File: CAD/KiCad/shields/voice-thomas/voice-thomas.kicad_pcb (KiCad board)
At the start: 2 copper layers, 30 x 42 mm, 20 parts

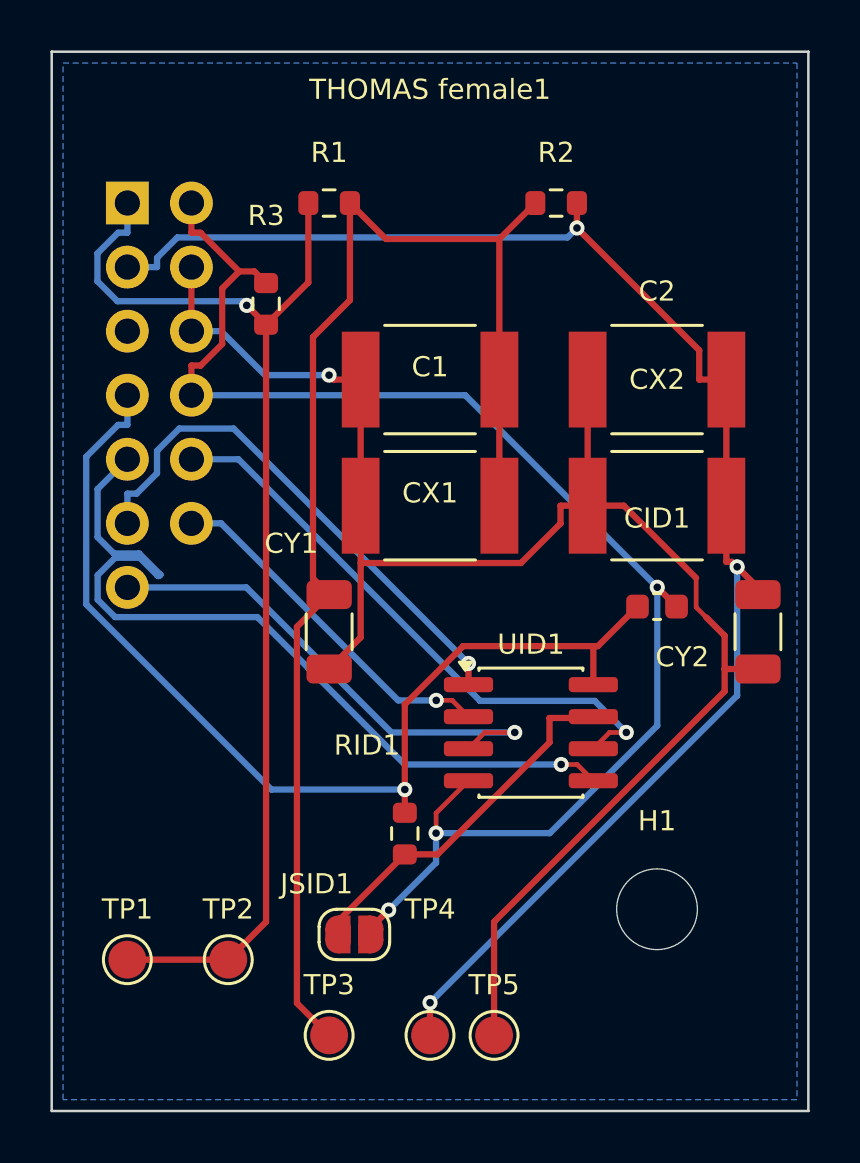
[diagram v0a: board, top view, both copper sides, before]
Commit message: Remove shield identification and adopt the simplified connector and Teensy pin maps
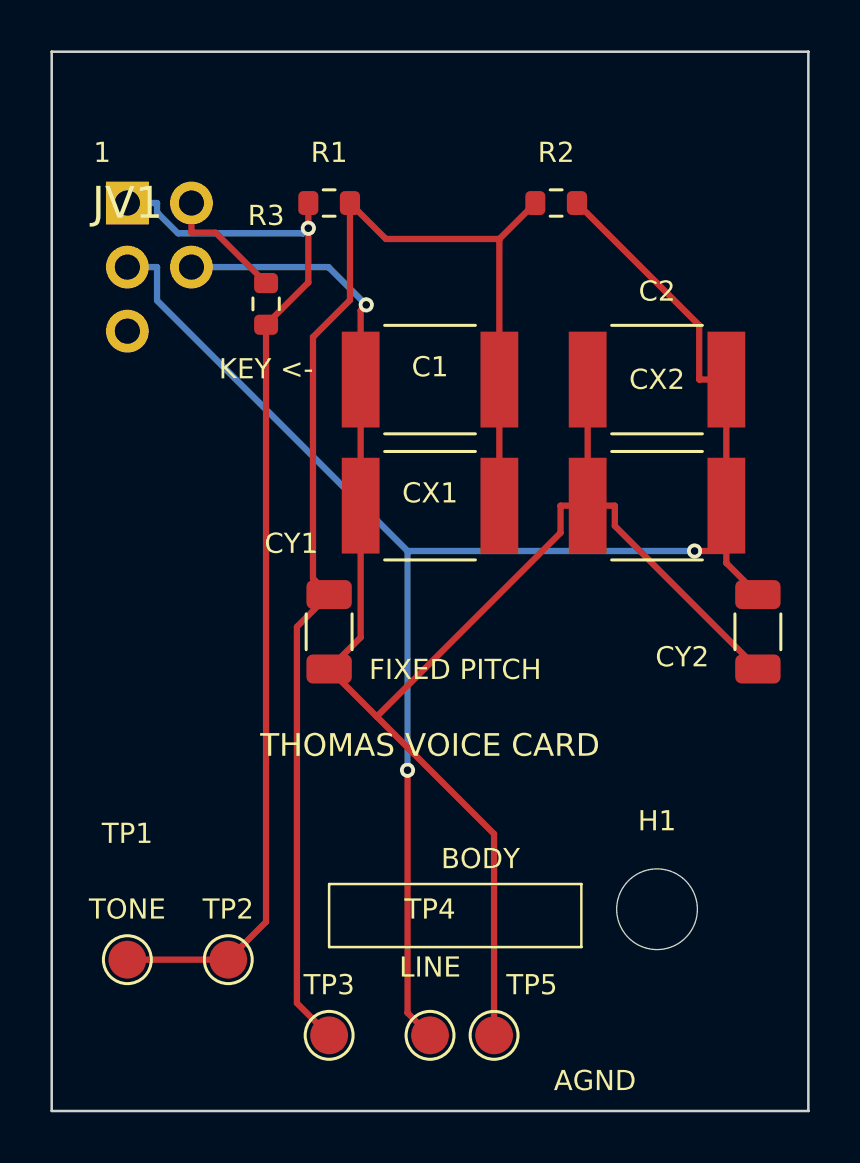
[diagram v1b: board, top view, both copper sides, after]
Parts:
- removed CID1: 100nF, Shields:C_0603_1608Metric
- removed JSID1: WRITE ENABLE - OPEN, Shields:SolderJumper-2_P1.3mm_Open_RoundedPad1.0x1.5mm
- removed RID1: 10K, Shields:R_0603_1608Metric
- removed UID1: M24C02-RMN6TP, Shields:SOIC-8_3.9x4.9mm_P1.27mm
- JV1: value VOICE - KEY 14 -> VOICE - KEY 6; footprint Shields:Socket_2x07_Key14 -> Shields:Socket_2x03_Key6
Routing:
- net GND: track 57.3 -> 4.96 mm, vias 3 -> 0
- net IOREF: track 41.5 -> 0.00 mm, vias 1 -> 0
- net shield/sda: track 33.4 -> 0.00 mm, vias 1 -> 0
- net shield/scl: track 23.3 -> 0.00 mm, vias 1 -> 0
- net addr0: track 21.0 -> 0.00 mm, vias 1 -> 0
- net addr2: track 19.8 -> 0.00 mm, vias 1 -> 0
- net id/wp: track 14.6 -> 0.00 mm
- net addr1: track 14.2 -> 0.00 mm, vias 1 -> 0
- net filter out: track 61.6 -> 67.9 mm, vias 3 -> 2
- net tone: track 46.5 -> 43.3 mm
- net AGND: track 66.6 -> 67.2 mm
- removed copper zone on B.Cu, net AGND
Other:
- board text added: "1"
- board text added: "1.2K"
- board text added: "1.8K"
- board text added: "10n"
- board text added: "150n"
- board text added: "2.2K"
- board text added: "220n"
- board text added: "2K"
- board text added: "470n"
- board text added: "47n"
- board text added: "AGND"
- board text added: "BODY"
- board text added: "BODY/Hz"
- board text added: "C1=C2"
- board text added: "F1 1012"
- board text added: "F2 2531"
- board text added: "F3 6329"
- board text added: "FIT"
- board text added: "FIXED PITCH"
- board text added: "KEY <-"
- board text added: "LINE"
- board text added: "M1 162"
- board text added: "M2 405"
- board text added: "R1=R2"
- board text added: "THOMAS VOICE CARD"
- board text added: "TONE"
- board text removed: "THOMAS female1"

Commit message: Finish revised shield routing, printed identification and clean KiCad checks
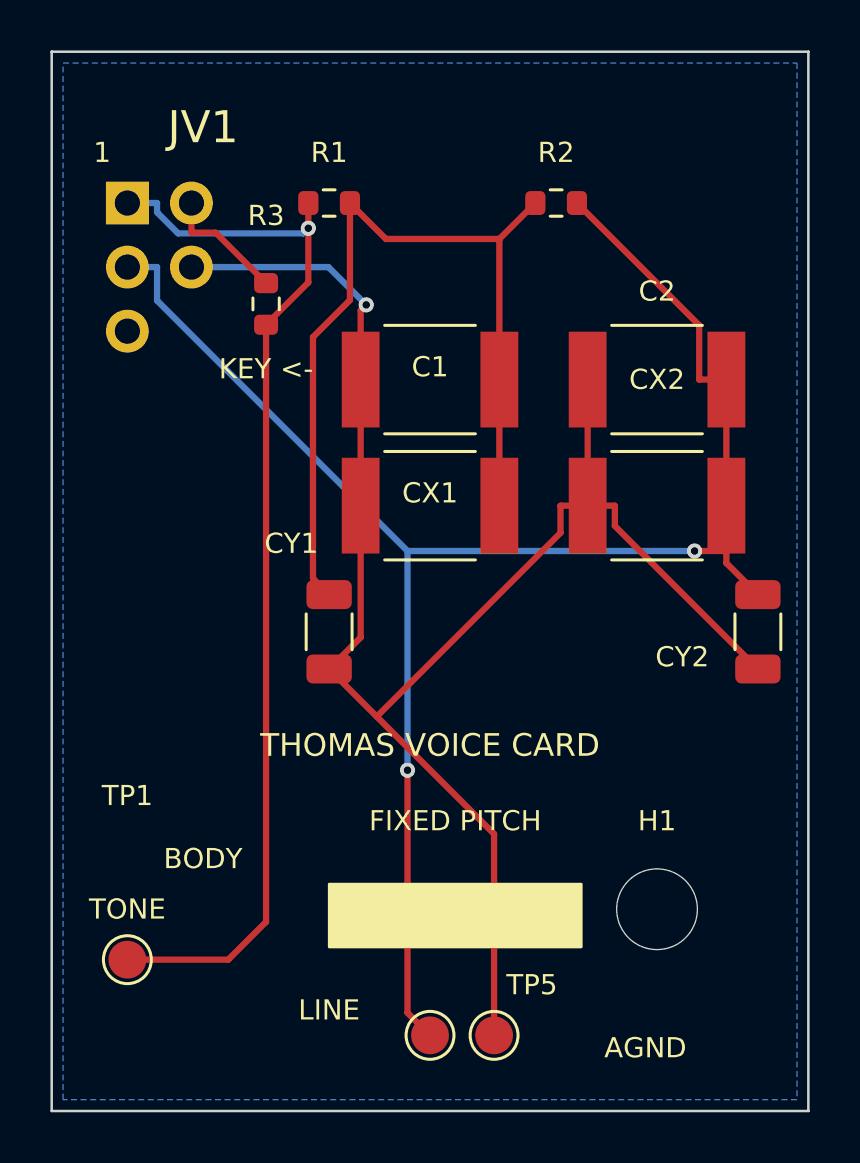
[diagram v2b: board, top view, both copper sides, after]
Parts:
- removed TP2: tone, Shields:TestPoint_Pad_D1.5mm
- removed TP3: stage1, Shields:TestPoint_Pad_D1.5mm
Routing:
- net stage1: track 54.0 -> 35.5 mm
- added copper zone on B.Cu, net AGND

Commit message: Update shields for Thomas RC cards, debug headers and body microphones
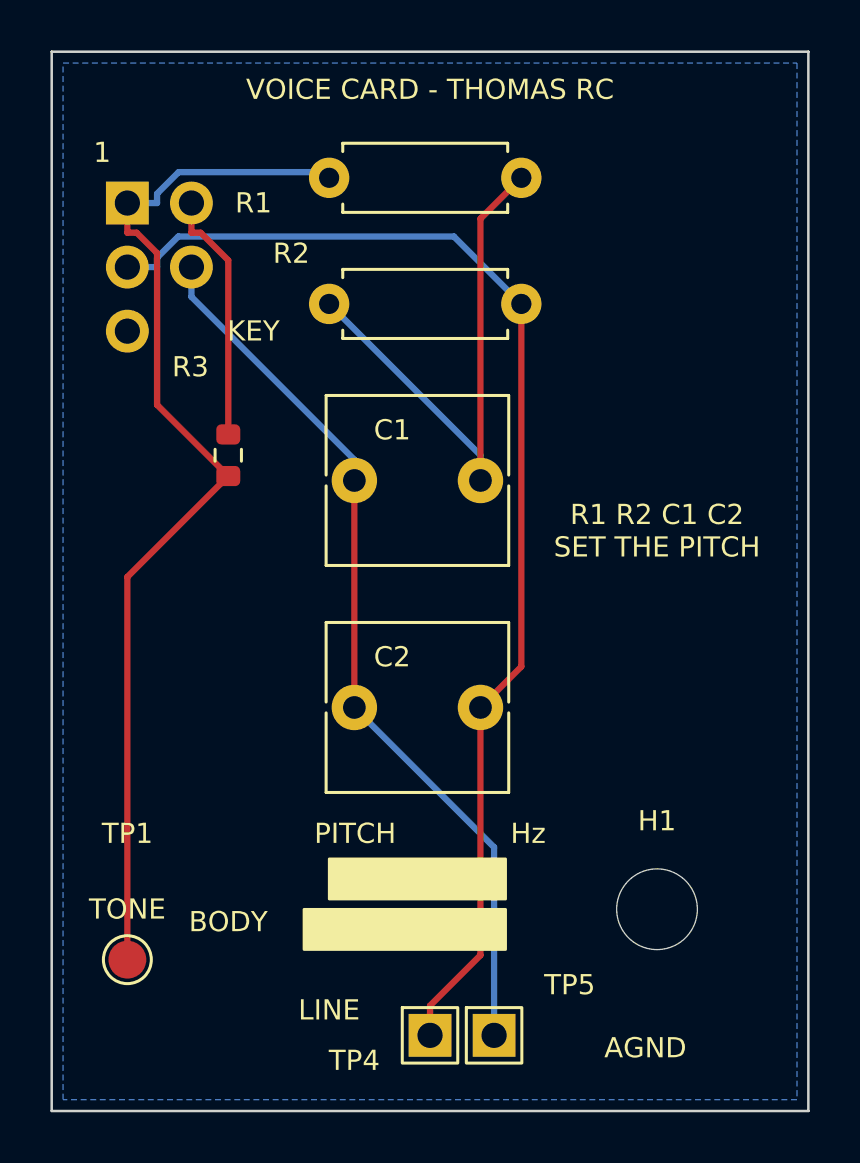
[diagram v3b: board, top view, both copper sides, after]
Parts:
- removed CX1, CX2: DNP PPS, Shields:PPS_6041
- removed CY1, CY2: DNP C0G, Shields:C_1206_3216Metric
- C1, C2: value 150nF PPS -> 150nF film 5% >=50V; footprint Shields:PPS_6041 -> Shields:C_Rect_L7.0mm_W6.5mm_P5.00mm
- R1, R2: value 1K2 -> 1K2 1% 0.25W; footprint Shields:R_0603_1608Metric -> Shields:R_Axial_DIN0207_L6.3mm_D2.5mm_P7.62mm_Horizontal
- TP4, TP5: footprint Shields:TestPoint_Pad_D1.5mm -> Shields:TestPin_1x01_P2.54mm
- moved C2 17.7 mm to (62.0, 76.0)
- moved R2 9.85 mm to (61.0, 60.0)
- moved R3 6.18 mm to (57.0, 66.0)
- moved C1 5.00 mm to (62.0, 67.0)
- moved R1 1.00 mm to (61.0, 55.0)
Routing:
- net AGND: track 67.2 -> 35.4 mm, vias 1 -> 0
- net filter out: track 67.9 -> 47.9 mm, vias 2 -> 0
- net stage1: track 35.5 -> 22.2 mm
- net GND: track 4.96 -> 10.00 mm
- net tone: track 43.3 -> 42.3 mm, vias 1 -> 0
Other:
- board text added: "1000 1K8 100n"
- board text added: "11314 1K6 10n"
- board text added: "1414 2K7 47n"
- board text added: "177 2K2 470n"
- board text added: "2000 2K7 33n"
- board text added: "250 2K2 330n"
- board text added: "2828 2K 33n"
- board text added: "354 2K2 220n"
- board text added: "4000 2K 22n"
- board text added: "500 2K4 150n"
- board text added: "5657 2K2 15n"
- board text added: "707 2K4 100n"
- board text added: "8000 2K2 10n"
- board text added: "F1 1012 1K2 150n"
- board text added: "F2 2531 1K8 47n"
- board text added: "F3 6329 2K2 10n"
- board text added: "KEY"
- board text added: "M1 162 2K2 470n"
- board text added: "M2 405 2K 220n"
- board text added: "PITCH Hz"
- board text added: "R x C = 0.179 / f"
- board text added: "R1 R2 C1 C2 SET THE PITCH"
- board text added: "VOICE CARD - THOMAS RC"
- board text removed: "1.2K"
- board text removed: "1.8K"
- board text removed: "10n"
- board text removed: "150n"
- board text removed: "2.2K"
- board text removed: "220n"
- board text removed: "2K"
- board text removed: "470n"
- board text removed: "47n"
- board text removed: "BODY/Hz"
- board text removed: "C1=C2"
- board text removed: "F1 1012"
- board text removed: "F2 2531"
- board text removed: "F3 6329"
- board text removed: "FIT"
- board text removed: "FIXED PITCH"
- board text removed: "KEY <-"
- board text removed: "M1 162"
- board text removed: "M2 405"
- board text removed: "R1=R2"
- board text removed: "THOMAS VOICE CARD"
